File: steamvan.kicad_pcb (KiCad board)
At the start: 2 copper layers, 243.4 x 76.7 mm, 188 parts, among them J1 Conn_01x05_Male, Q1 FMMT493TA, SW1 SW_Push, U1 STM32F303CBTx, U2 TLV70233_SOT23-5, U3 NUF2221W1T2G, U4 74LVC1G34, Y1 8MHz

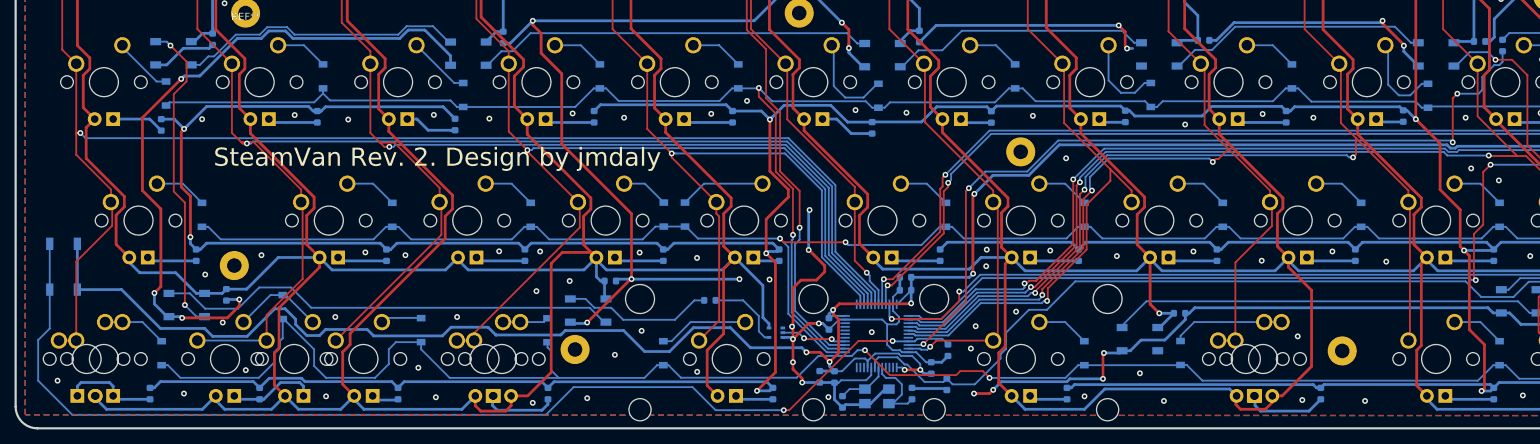
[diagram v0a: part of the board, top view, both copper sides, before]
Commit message: Update: Move reset switch to line up better with case
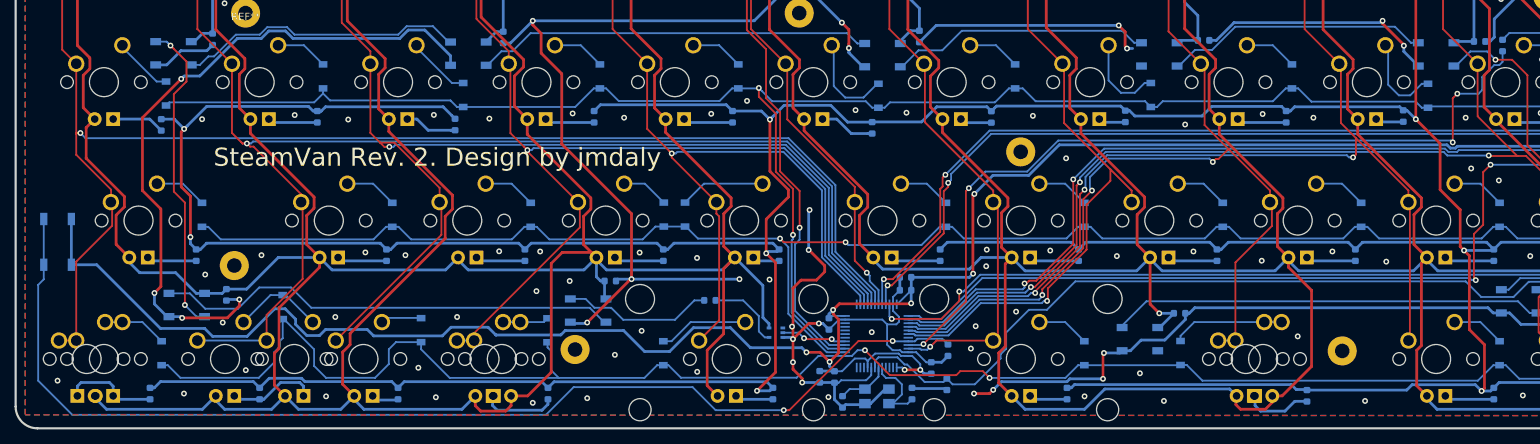
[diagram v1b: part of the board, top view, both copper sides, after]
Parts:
- moved SW1 3.51 mm to (77.0, 106.1)
- moved R43 1.93 mm to (248.9, 127.3)
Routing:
- net Net-(RC8-Pad1): track 154.0 -> 157.1 mm
- net +3V3: track 352.8 -> 355.1 mm
- net Net-(K_RALT1-Pad4): track 11.4 -> 9.36 mm
- net COL1: track 178.4 -> 177.1 mm
- net LEDGND: track 951.8 -> 950.5 mm
- net GND: vias 122 -> 121

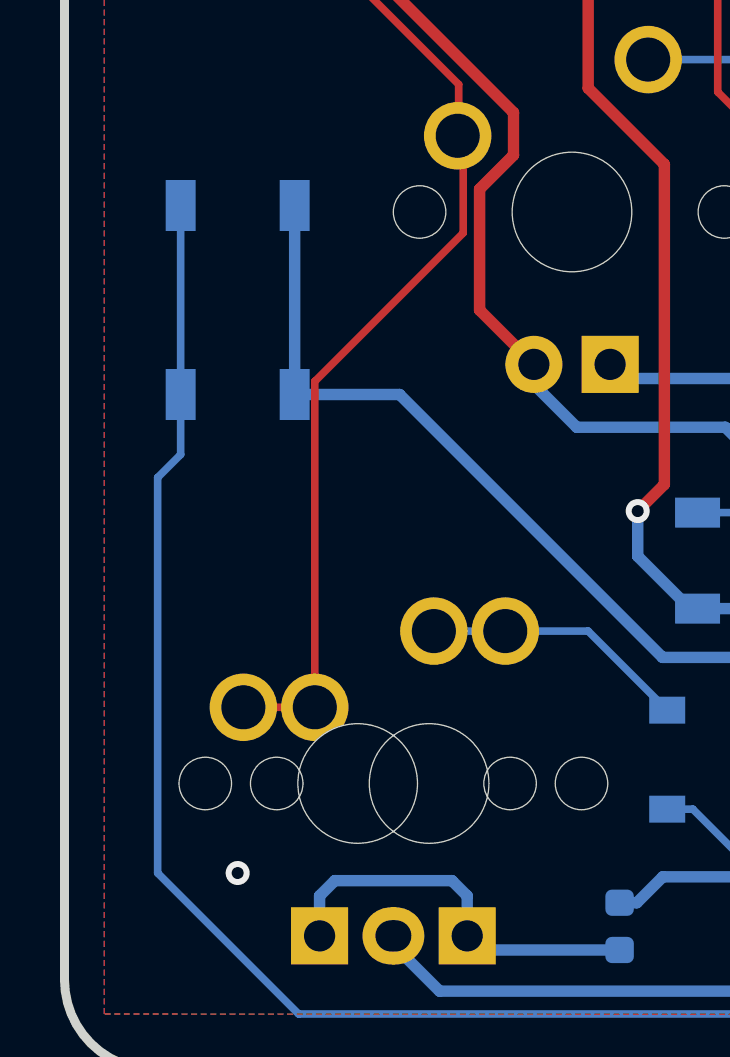
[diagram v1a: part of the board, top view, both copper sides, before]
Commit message: Update: Move reset switch in from edge a bit
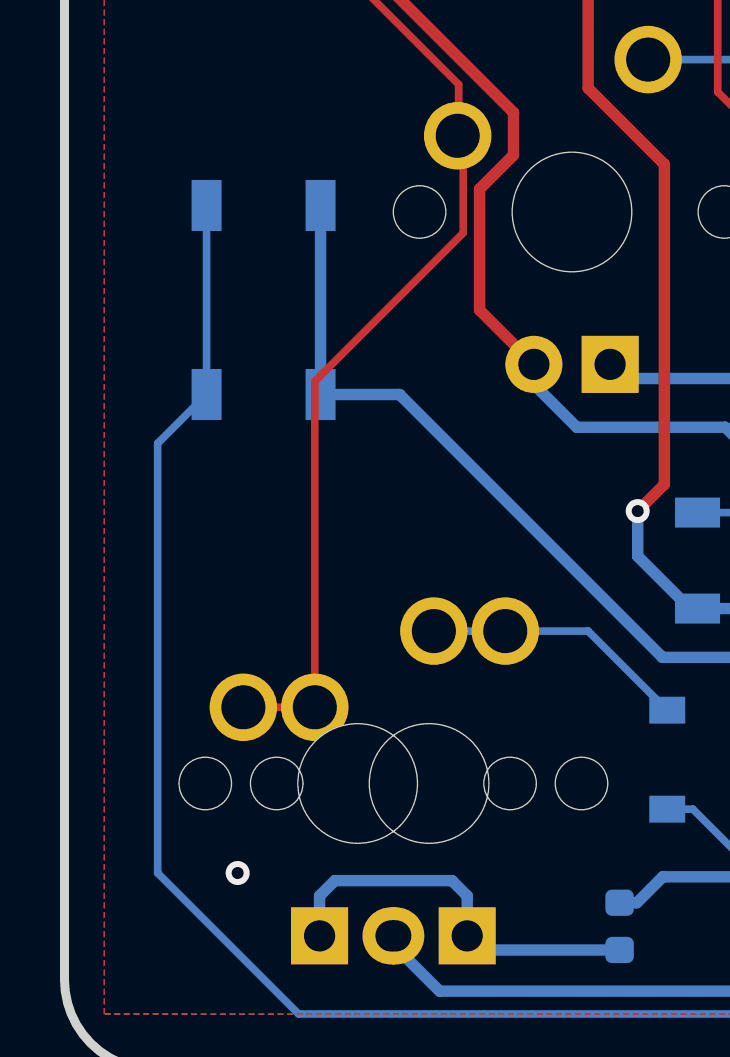
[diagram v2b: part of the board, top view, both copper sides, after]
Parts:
- moved SW1 0.86 mm to (77.8, 106.1)
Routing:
- net +3V3: track 355.1 -> 354.2 mm
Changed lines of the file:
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@@
     (thickness 1.6)
     (drawings 6)
-    (tracks 2168)
+    (tracks 2167)
     (zones 0)
     (modules 188)
@@
   )
   (module Button_Switch_SMD:SW_SPST_TL3342 (layer B.Cu)
-    (at 76.962 106.1212 90)
+    (at 77.8256 106.1212 90)
     (descr "Low-profile SMD Tactile Switch, https://www.e-switch.com/system/asset/product_line/data_sheet/165/TL3342.pdf")
     (tags "SPST Tactile Switch")
@@
   (segment (start 91.1225 118.0338) (end 82.3599 109.2712) (width 0.381) (layer B.Cu) (net 4))
   (segment (start 169.5704 117.9322) (end 164.4777 117.9322) (width 0.381) (layer B.Cu) (net 4))
-  (segment (start 82.3599 109.2712) (end 78.862 109.2712) (width 0.381) (layer B.Cu) (net 4))
   (segment (start 154.8765 118.3259) (end 146.8374 118.3259) (width 0.381) (layer B.Cu) (net 4))
   (segment (start 164.4777 117.9322) (end 161.2011 121.2088) (width 0.381) (layer B.Cu) (net 4))
@@
   (segment (start 287.274 80.772) (end 290.6776 80.772) (width 0.381) (layer B.Cu) (net 4))
   (segment (start 290.6776 80.772) (end 292.989 83.0834) (width 0.381) (layer B.Cu) (net 4))
-  (segment (start 78.862 102.9712) (end 78.862 109.2712) (width 0.381) (layer B.Cu) (net 4))
+  (segment (start 79.7256 102.9712) (end 79.7256 109.2712) (width 0.381) (layer B.Cu) (net 4))
+  (segment (start 82.3599 109.2712) (end 79.7256 109.2712) (width 0.381) (layer B.Cu) (net 4))
   (via (at 312.3692 112.2426) (size 0.8) (drill 0.4) (layers F.Cu B.Cu) (net 5))
   (segment (start 312.6359 70.1929) (end 310.896 68.453) (width 0.254) (layer F.Cu) (net 5) (status 20))
@@
   (segment (start 195.316539 119.456211) (end 194.96025 119.8125) (width 0.254) (layer B.Cu) (net 98))
   (segment (start 198.729711 119.456211) (end 195.316539 119.456211) (width 0.254) (layer B.Cu) (net 98))
-  (segment (start 75.062 111.2724) (end 75.062 109.2712) (width 0.254) (layer B.Cu) (net 98))
-  (segment (start 74.295 112.0394) (end 75.062 111.2724) (width 0.254) (layer B.Cu) (net 98))
+  (segment (start 75.9256 102.9712) (end 75.9256 109.2712) (width 0.254) (layer B.Cu) (net 98))
+  (segment (start 74.295 110.9018) (end 75.9256 109.2712) (width 0.254) (layer B.Cu) (net 98))
+  (segment (start 167.5384 129.286) (end 164.3634 126.111) (width 0.254) (layer B.Cu) (net 98))
   (segment (start 176.911 129.286) (end 167.5384 129.286) (width 0.254) (layer B.Cu) (net 98))
-  (segment (start 74.295 125.222) (end 74.295 112.0394) (width 0.254) (layer B.Cu) (net 98))
+  (segment (start 74.295 125.222) (end 74.295 110.9018) (width 0.254) (layer B.Cu) (net 98))
   (segment (start 164.3634 126.111) (end 147.9931 126.111) (width 0.254) (layer B.Cu) (net 98))
   (segment (start 147.9931 126.111) (end 144.1831 129.921) (width 0.254) (layer B.Cu) (net 98))
   (segment (start 144.1831 129.921) (end 78.994 129.921) (width 0.254) (layer B.Cu) (net 98))
-  (segment (start 167.5384 129.286) (end 164.3634 126.111) (width 0.254) (layer B.Cu) (net 98))
   (segment (start 78.994 129.921) (end 74.295 125.222) (width 0.254) (layer B.Cu) (net 98))
-  (segment (start 75.062 102.9712) (end 75.062 109.2712) (width 0.254) (layer B.Cu) (net 98))
   (segment (start 190.45625 114.7125) (end 190.45625 111.485) (width 0.254) (layer B.Cu) (net 105) (status 10))
   (via (at 190.68646 111.25479) (size 0.8) (drill 0.4) (layers F.Cu B.Cu) (net 105))

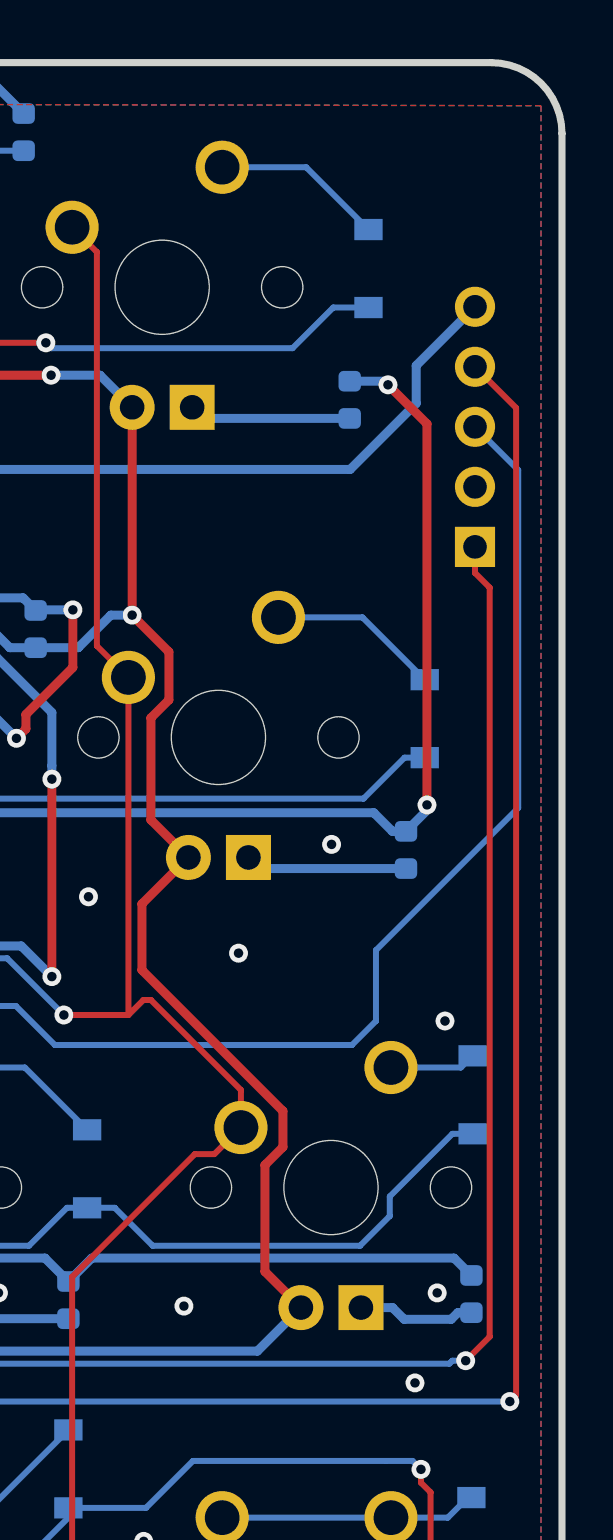
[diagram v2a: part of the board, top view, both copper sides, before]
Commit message: Update: move programming headers - also regenerate Gerbers
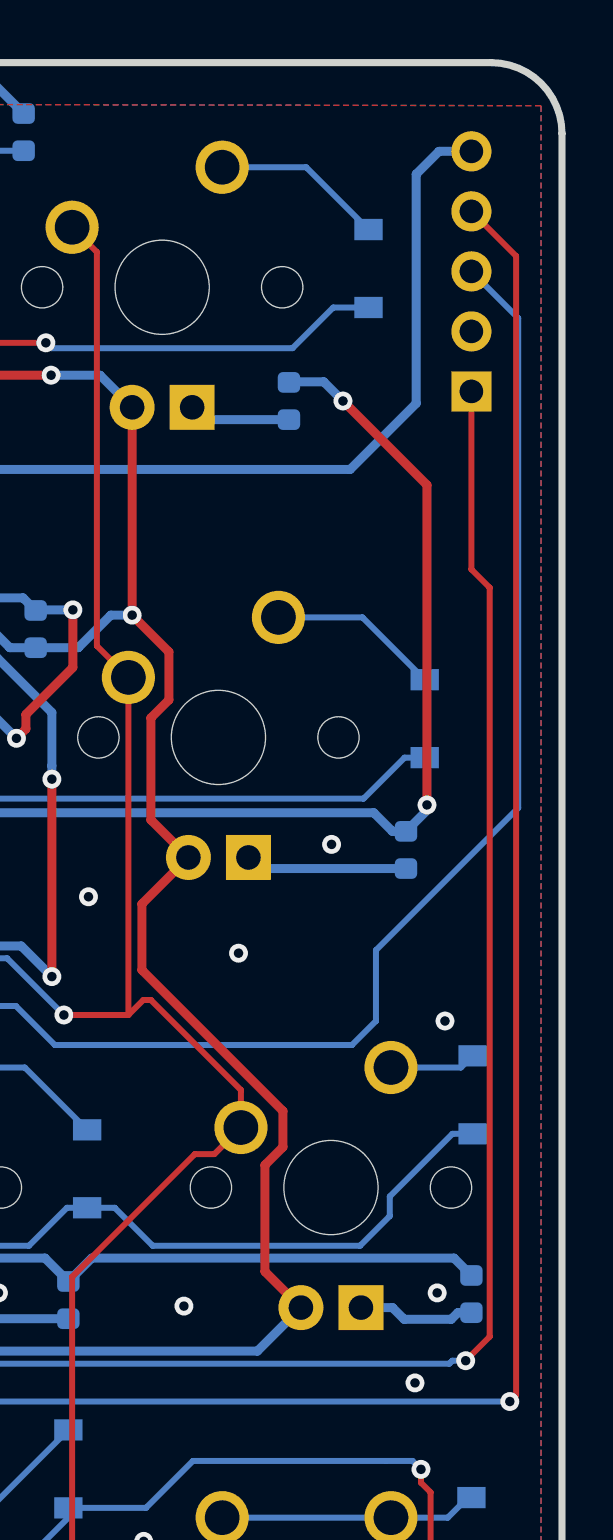
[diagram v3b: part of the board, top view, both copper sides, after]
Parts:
- moved J1 6.58 mm to (310.7, 69.5)
- moved R12 2.57 mm to (303.0, 69.9)
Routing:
- net +3V3: track 354.2 -> 361.5 mm
- net SWDIO: track 159.3 -> 166.0 mm
- net SWCLK: track 159.7 -> 166.3 mm
- net NRST: track 180.1 -> 186.7 mm
- net Net-(K_BACK1-Pad4): track 6.86 -> 4.31 mm
- net LEDGND: track 950.5 -> 951.6 mm

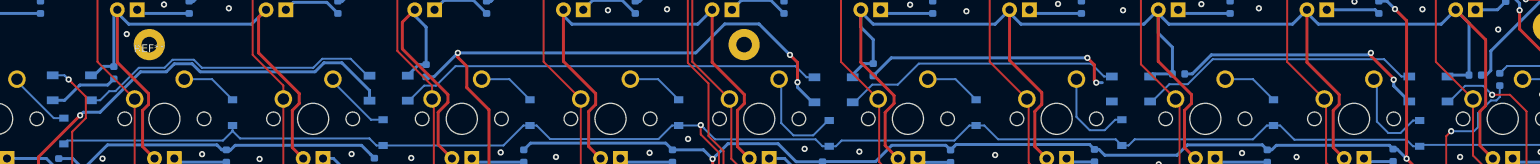
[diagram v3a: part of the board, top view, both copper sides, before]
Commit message: Update: adjust top row RGB LEDs
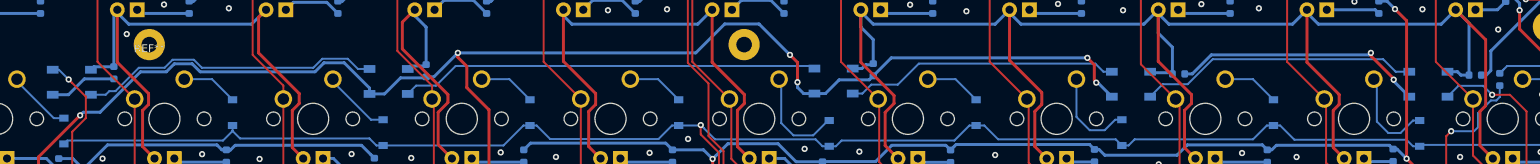
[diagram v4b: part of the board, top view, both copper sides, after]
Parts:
- moved RGB5 1.12 mm to (190.5, 79.3)
- moved RGB4 0.86 mm to (133.5, 79.3)
- moved RGB3 0.71 mm to (92.9, 79.5)
- moved RGB6 0.61 mm to (228.6, 79.7)
- moved RGB7 0.61 mm to (266.7, 79.7)
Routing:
- net GND: track 540.5 -> 557.1 mm
- net +5V: track 1346.6 -> 1345.4 mm
- net Net-(RGB4-Pad2): track 54.5 -> 53.7 mm
- net Net-(RGB5-Pad2): track 35.9 -> 35.2 mm
- net Net-(RGB3-Pad2): track 39.6 -> 39.0 mm
- net Net-(RGB6-Pad2): track 36.4 -> 35.9 mm

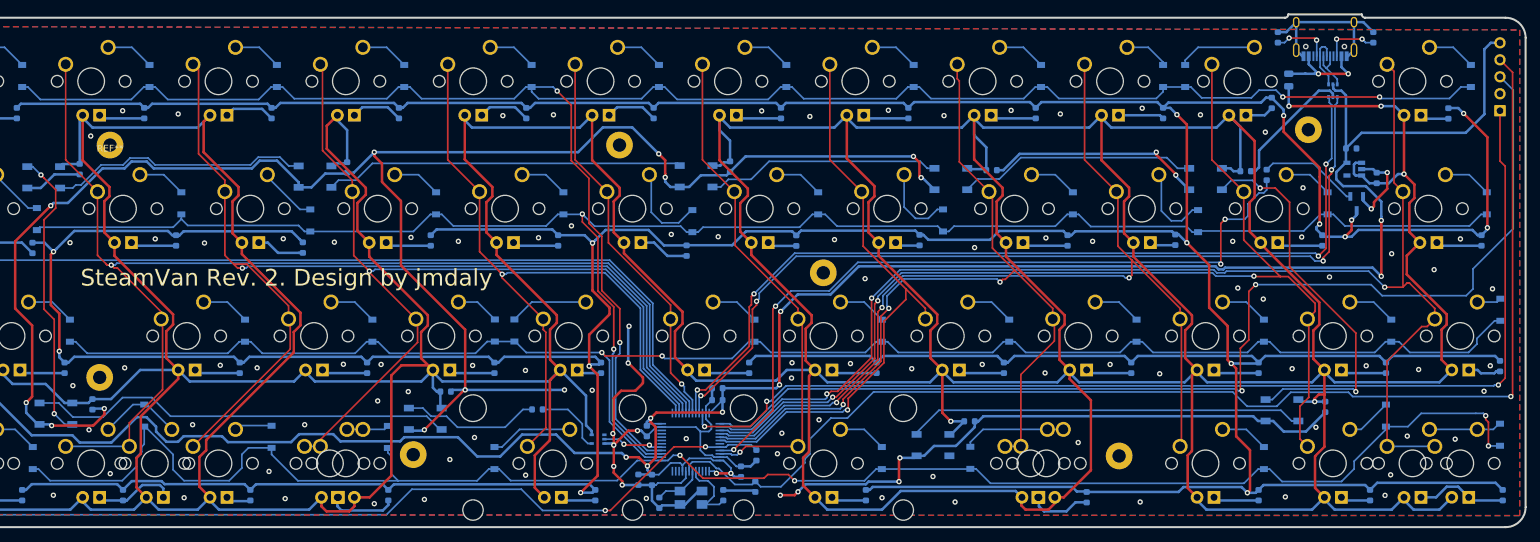
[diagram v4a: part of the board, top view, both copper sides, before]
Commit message: Update: move programming jumper
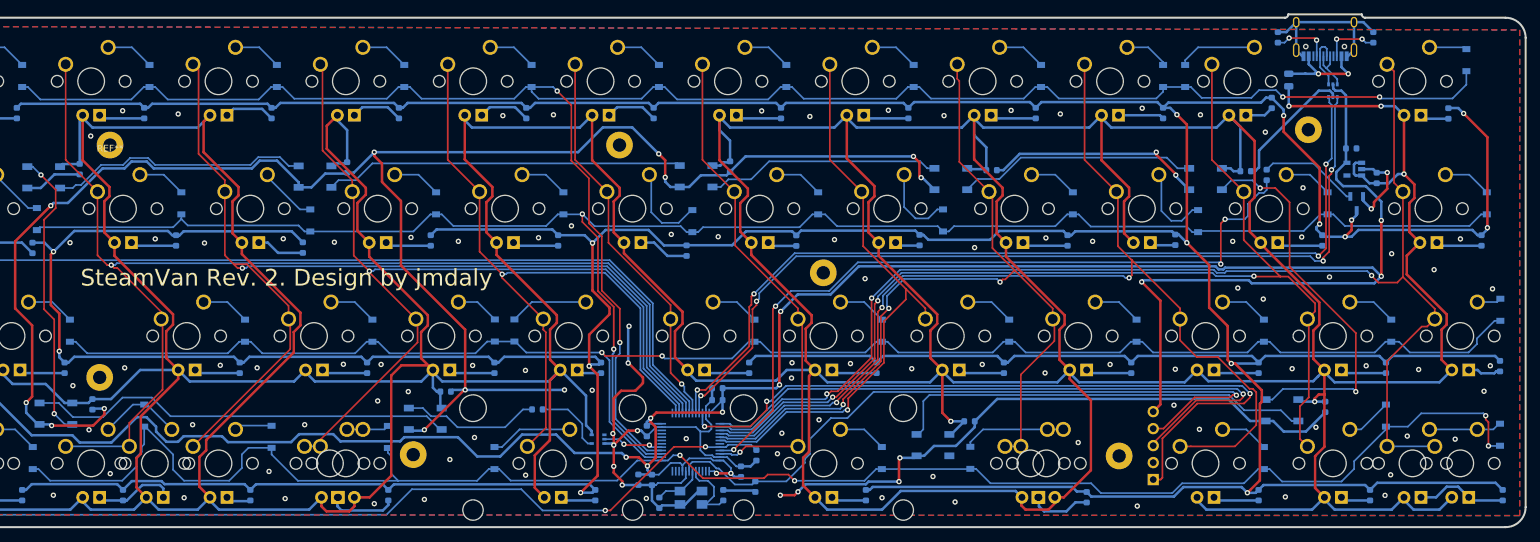
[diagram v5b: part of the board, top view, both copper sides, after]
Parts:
- moved J1 75.7 mm to (258.9, 124.7)
- moved D12 2.46 mm to (305.7, 61.9)
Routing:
- net NRST: track 186.7 -> 106.5 mm
- net SWCLK: track 166.3 -> 98.2 mm, vias 2 -> 1
- net SWDIO: track 166.0 -> 111.1 mm
- net +5V: track 1345.4 -> 1301.0 mm
- net +3V3: track 361.5 -> 383.8 mm, vias 10 -> 11
- net COL9: track 142.9 -> 159.1 mm
- net Net-(RGB8-Pad2): track 59.4 -> 63.6 mm
- net LEDGND: track 951.6 -> 953.9 mm
- net GND: track 557.1 -> 559.2 mm, vias 121 -> 123
- net Net-(D12-Pad2): track 7.28 -> 5.63 mm
- net ROW0: track 299.3 -> 300.8 mm
- net COL11: track 191.2 -> 189.8 mm
- net ROW3: track 260.3 -> 261.5 mm
